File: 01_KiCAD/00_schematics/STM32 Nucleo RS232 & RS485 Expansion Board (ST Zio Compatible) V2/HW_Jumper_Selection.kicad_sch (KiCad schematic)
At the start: 69 parts, among them J11 MODE0, J12 MODE1, J13 MODE2, J14 DIR, J15 TERM_TX, J16 TERM_RX, J17 SLR, U6 SN74LVC14ADR, U7 SN74LVC14ADR, U8 SN74LVC2G14DBV

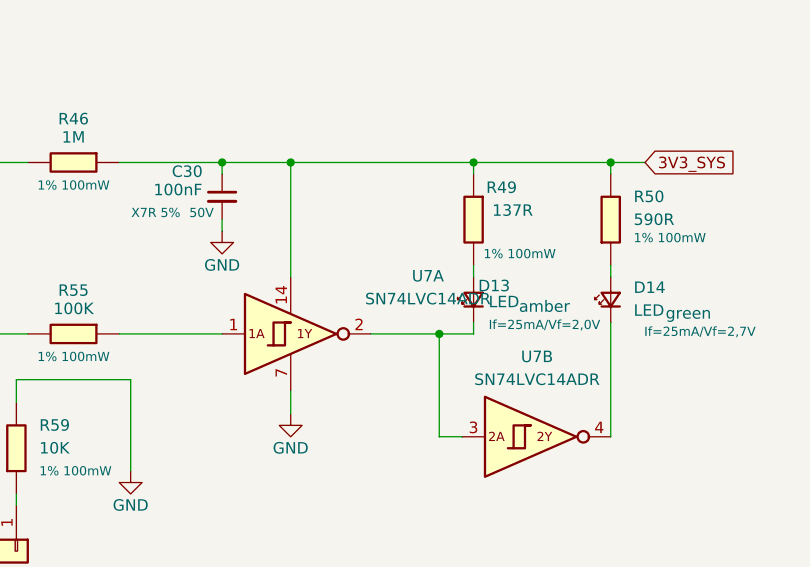
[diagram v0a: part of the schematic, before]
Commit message: Small changes to schematics & PCB work
Made some minor adjustments to the schematics, updated the PCB accordingly.
Placed all the components on the board and did some of the routing.
Updated the 3D models of all the components.
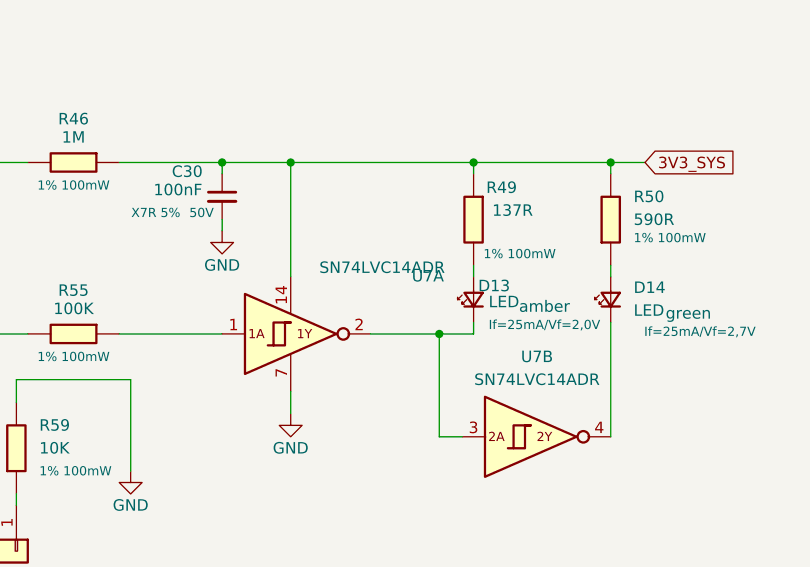
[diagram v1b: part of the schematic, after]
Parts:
- C29, C30, C31: footprint PCM_SparkFun-Capacitor:C_0603_1608Metric -> Capacitor_SMD:C_0805_2012Metric
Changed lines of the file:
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@@
 			)
 		)
-		(property "Footprint" "PCM_SparkFun-Capacitor:C_0603_1608Metric"
+		(property "Footprint" "Capacitor_SMD:C_0805_2012Metric"
 			(at 77.47 137.16 0)
 			(effects
@@
 			)
 		)
-		(property "Footprint" "PCM_SparkFun-Capacitor:C_0603_1608Metric"
+		(property "Footprint" "Capacitor_SMD:C_0805_2012Metric"
 			(at 77.47 52.07 0)
 			(effects
@@
 		(on_board yes)
 		(dnp no)
-		(fields_autoplaced yes)
 		(property "Reference" "U7"
 			(at 100.33 134.5498 0)
@@
 		)
 		(property "Value" "SN74LVC14ADR"
-			(at 100.33 137.0898 0)
+			(at 95.25 133.604 0)
 			(effects
 				(font
@@
 			)
 		)
-		(property "Footprint" "PCM_SparkFun-Capacitor:C_0603_1608Metric"
+		(property "Footprint" "Capacitor_SMD:C_0805_2012Metric"
 			(at 77.47 222.25 0)
 			(effects

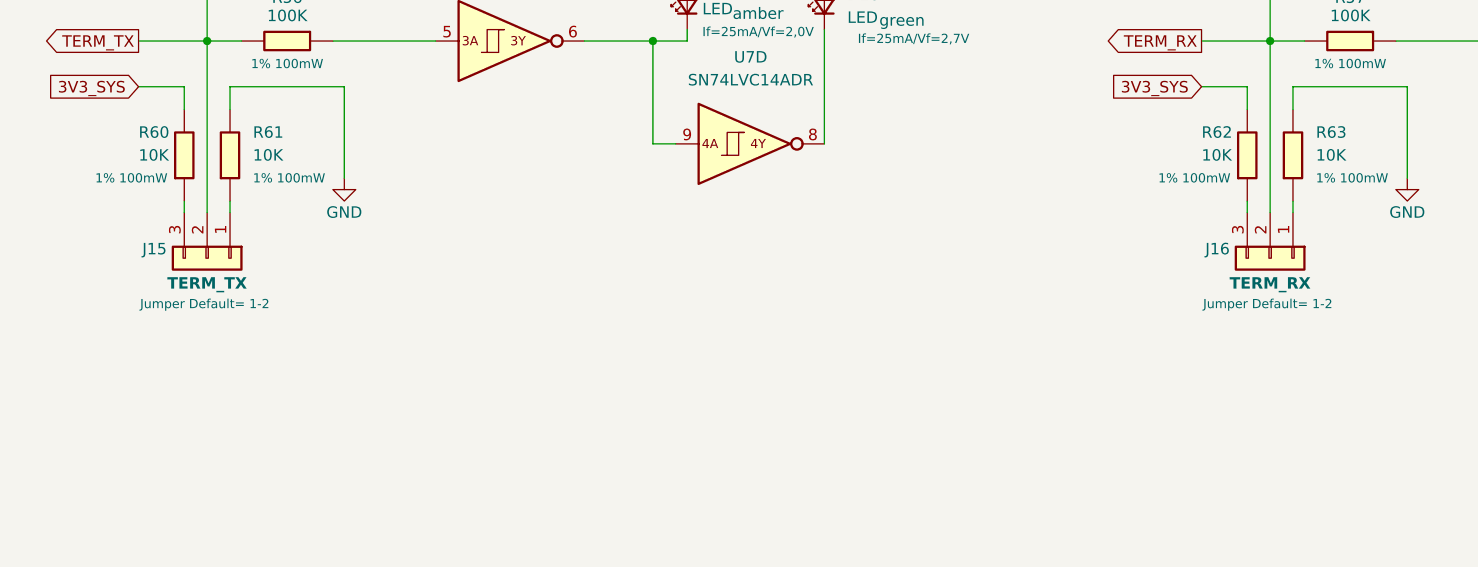
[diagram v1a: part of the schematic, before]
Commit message: Finalizing board layout & routing
Set HW Revision of board to: HW REV A0.1 and placed this as copper text on the back of the PCB.
Run DRC to see any critical errors. Resolved some minor silkscreen issues with overlapping text.
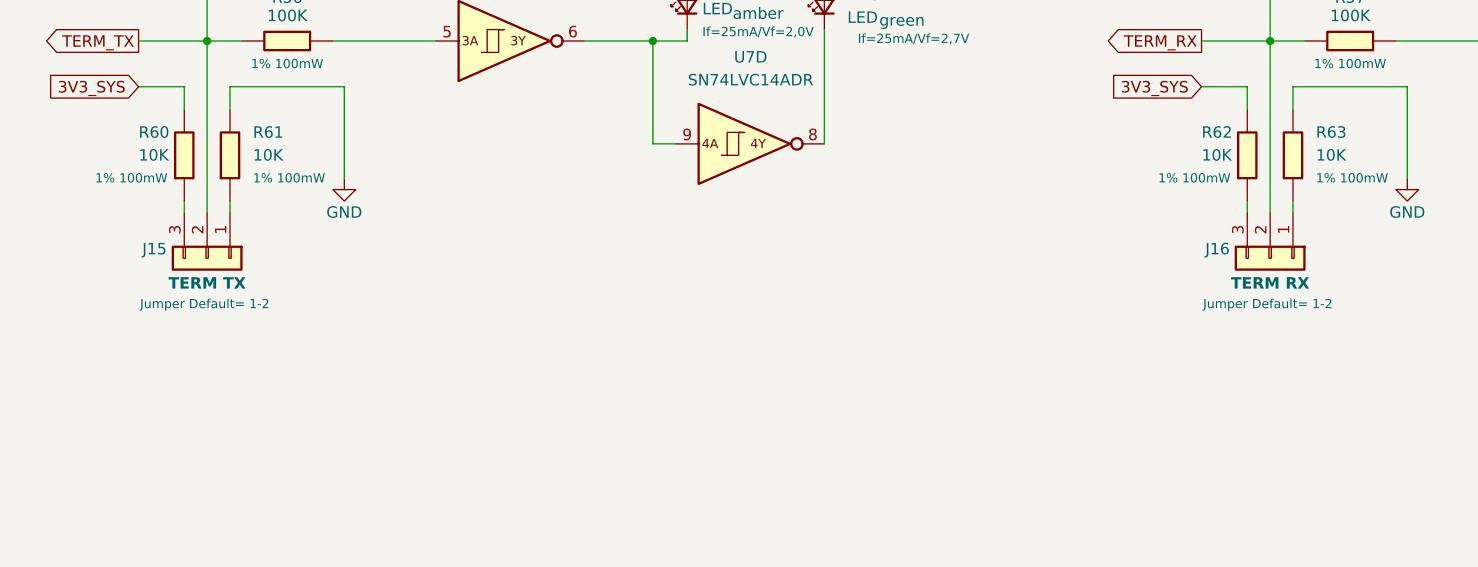
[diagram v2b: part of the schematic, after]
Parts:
- J15: value TERM_TX -> TERM TX
- J16: value TERM_RX -> TERM RX
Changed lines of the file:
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@@
 			)
 		)
-		(property "Value" "TERM_TX"
+		(property "Value" "TERM TX"
 			(at 170.18 167.894 90)
 			(effects
@@
 			)
 		)
-		(property "Value" "TERM_RX"
+		(property "Value" "TERM RX"
 			(at 288.29 167.894 90)
 			(effects

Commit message: Final revision checkup
After BOM-update and corrected some footprints and package sizes for resistors and capacitors, updated the PCB to "HW REV A0.2" as final PCB layout. Need to run DRC check before final approval.
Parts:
- C29, C30, C31: Dielectric X7R 5% -> X7R; LCSC C91183 -> C2167095; MPN CC0603JRX7R9BB104 -> C0805C104J5RACTU; Manufacturer YAGEO -> KEMET; Mouser PN (none) -> 80-C0805C104J5R; Package 0603 -> 0805; Tolerance 20% -> 5%; Voltage 25V -> 50V
- D10, D12, D14, D16, D18, D20, D8: Color green -> Green; Mouser PN (none) -> 743-IN-S63AT5G; Voltage (none) -> 2,7V
- D11, D13, D15, D17, D19, D7, D9: Color amber -> Amber; Mouser PN (none) -> 743-IN-S63AT5A; Voltage (none) -> 2,0V
- J11, J12, J13, J14, J15, J16, J17: LCSC C6631883 -> C5714562; Mouser PN (none) -> 200-HTSW10307GS
- R28, R29, R30, R46, R47, R48, R64: LCSC C14675 -> C20142017; MPN RC0603FR-071ML -> AC0603FR-7W1ML; Mouser PN (none) -> 603-AC0603FR-7W1ML; Package C105578 -> 0603
- R31, R33, R35, R49, R51, R53, R65: LCSC C227580 -> C227579; MPN AC0603FR-07137RL -> AC0603FR-07137KL; Mouser PN (none) -> 603-AC0603FR-07137KL
- R32, R34, R36, R50, R52, R54, R66: LCSC C22548 -> C227973; MPN RC0603FR-071KL -> AC0603FR-07590RL; Mouser PN (none) -> 603-AC0603FR-07590RL
- R37, R38, R39, R55, R56, R57, R67: LCSC C14675 -> C5552302; MPN RC0603FR-07100KL -> AC0603FR-7W100KL; Mouser PN (none) -> 603-AC0603FR-7W100KL
- R40, R41, R42, R43, R44, R45, R58, R59, R60, R61, R62, R63, R68, R69: LCSC C98220 -> C20142011; MPN RC0603FR-0710KL -> AC0603FR-7W10KL; Mouser PN (none) -> 603-AC0603FR-7W10KL
- U6, U7: LCSC (none) -> C133541; MPN (none) -> SN74LVC14ADR; Manufacturer (none) -> TI; Mouser PN (none) -> 595-SN74LVC14ADR; Package (none) -> SOIC-14; Type (none) -> SMD
- U8: LCSC (none) -> C12401; MPN (none) -> SN74LVC2G14DBVR; Manufacturer (none) -> TI; Mouser PN (none) -> 595-SN74LVC2G14DBVR; Package (none) -> SOT-23-6; Type (none) -> SMD

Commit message: Changed to HR_REVA0.3
Updates design to PCB HW-REVA0.3 with the folowing changes:

CL_HW_2026_0001
Replaced text on silkscreen D3=>RX and D4=>TX.

CL_HW_2026_0002
Changed MCU_SHDN pin for THVD4431 from CN9-30 to CN9-11 to make it also Arduino compatible
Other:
- note added: "Stroom door Amber LED: I=U/R => 3,3V / 137Ω = 24mA Stroom door Groene LED: I=U/R => 3,3V / 590R = 5,6mA Maximale stroom door Schmit trigger: ±90mA"
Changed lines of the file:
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@@
 		(comment 3 "Initial revision")
+	)
+	(text "Stroom door Amber LED: I=U/R => 3,3V / 137Ω = 24mA\nStroom door Groene LED: I=U/R => 3,3V / 590R = 5,6mA\n\nMaximale stroom door Schmit trigger: ±90mA"
+		(exclude_from_sim no)
+		(at 105.918 26.162 0)
+		(effects
+			(font
+				(size 1.27 1.27)
+			)
+			(justify left)
+		)
 	)
 	(junction
